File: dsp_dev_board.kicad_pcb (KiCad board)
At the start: 4 copper layers, 100 x 100 mm, 92 parts, among them J1 aux_mcu_power, J10 DX07S016JA1R1500, J11 Conn_02x11_Odd_Even, J2 audio_in, J3 audio_out, J4 9v_jack, J5 input_jack, J6 output_jack, J7 digital, J8 analog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

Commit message: pcb: minor movements, add more labels
more silkscreens, move some traces
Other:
- board text added: "3.3V"
- board text added: "GND"
- board text added: "WM8731"
- board text added: "audio in"
- board text added: "audio out"
- board text added: "input"
- board text added: "output"
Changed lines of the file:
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@@
   (general
     (thickness 1.6)
-    (drawings 47)
-    (tracks 806)
+    (drawings 55)
+    (tracks 810)
     (zones 0)
     (modules 92)
@@
     (tags resistor)
     (attr smd)
-    (fp_text reference R4 (at 0 -1.43) (layer F.SilkS)
+    (fp_text reference R4 (at -0.025 1.5) (layer F.SilkS)
       (effects (font (size 1 1) (thickness 0.15)))
     )
@@
     (descr "Through hole straight pin header, 1x02, 2.54mm pitch, single row")
     (tags "Through hole pin header THT 1x02 2.54mm single row")
-    (fp_text reference J2 (at 3.2 0) (layer F.SilkS)
+    (fp_text reference J2 (at 0 5.2) (layer F.SilkS)
       (effects (font (size 1 1) (thickness 0.15)))
     )
@@
     (descr "Through hole straight pin header, 1x02, 2.54mm pitch, single row")
     (tags "Through hole pin header THT 1x02 2.54mm single row")
-    (fp_text reference J1 (at 3.1 0) (layer F.SilkS)
+    (fp_text reference J1 (at 0 5.2) (layer F.SilkS)
       (effects (font (size 1 1) (thickness 0.15)))
     )
@@
     )
   )
+  (gr_text output (at 100.4 68.5) (layer F.SilkS)
+    (effects (font (size 1 1) (thickness 0.15)))
+  )
+  (gr_text input (at 185.4 68.4) (layer F.SilkS)
+    (effects (font (size 1 1) (thickness 0.15)))
+  )
+  (gr_text GND (at 163.3 47.2) (layer F.SilkS)
+    (effects (font (size 1 1) (thickness 0.15)) (justify left))
+  )
+  (gr_text 3.3V (at 163.3 44.5325) (layer F.SilkS)
+    (effects (font (size 1 1) (thickness 0.15)) (justify left))
+  )
+  (gr_text "audio in" (at 173.5 69.8) (layer F.SilkS)
+    (effects (font (size 1 1) (thickness 0.15)) (justify left))
+  )
+  (gr_text WM8731 (at 163.2 79.5) (layer F.SilkS)
+    (effects (font (size 1 1) (thickness 0.15)) (justify left))
+  )
+  (gr_text GND (at 148.8275 70.1 -90) (layer F.SilkS)
+    (effects (font (size 1 1) (thickness 0.15)) (justify left))
+  )
+  (gr_text "audio out" (at 151.3675 70.1 -90) (layer F.SilkS)
+    (effects (font (size 1 1) (thickness 0.15)) (justify left))
+  )
   (gr_text PB07 (at 97.6 97.4125) (layer F.SilkS)
     (effects (font (size 1 1) (thickness 0.15)) (justify left))
@@
   (segment (start 153.631666 59.495) (end 154.125 59.495) (width 0.25) (layer F.Cu) (net 9) (status 30))
   (segment (start 149.02001 59.85001) (end 147.97 58.8) (width 0.25) (layer F.Cu) (net 9) (status 20))
-  (segment (start 153.76999 59.85001) (end 149.02001 59.85001) (width 0.25) (layer F.Cu) (net 9))
-  (segment (start 154.125 59.495) (end 153.76999 59.85001) (width 0.25) (layer F.Cu) (net 9) (status 10))
   (segment (start 148.315 60.585) (end 148.315 60.783334) (width 0.25) (layer F.Cu) (net 9) (status 30))
   (segment (start 149.02001 59.87999) (end 148.315 60.585) (width 0.25) (layer F.Cu) (net 9) (status 20))
   (segment (start 149.02001 59.85001) (end 149.02001 59.87999) (width 0.25) (layer F.Cu) (net 9))
+  (segment (start 149.64999 59.85001) (end 149.02001 59.85001) (width 0.25) (layer F.Cu) (net 9))
+  (segment (start 150.73999 59.85001) (end 149.64999 59.85001) (width 0.25) (layer F.Cu) (net 9))
+  (segment (start 154.125 59.495) (end 151.095 59.495) (width 0.25) (layer F.Cu) (net 9))
+  (segment (start 151.095 59.495) (end 150.73999 59.85001) (width 0.25) (layer F.Cu) (net 9))
   (segment (start 103.574999 60.225001) (end 93 60.225001) (width 0.25) (layer F.Cu) (net 10) (status 20))
   (segment (start 119.4 44.4) (end 103.574999 60.225001) (width 0.25) (layer F.Cu) (net 10))
@@
   (via (at 148.65 47.5) (size 0.4) (drill 0.3) (layers F.Cu B.Cu) (net 32))
   (segment (start 148.65 46.2) (end 148.65 47.45) (width 0.25) (layer F.Cu) (net 32) (status 10))
-  (segment (start 148.65 47.5) (end 145.474999 50.675001) (width 0.25) (layer B.Cu) (net 32))
-  (segment (start 145.474999 50.675001) (end 145.474999 52.725007) (width 0.25) (layer B.Cu) (net 32))
   (via (at 121.3 76.900006) (size 0.4) (drill 0.3) (layers F.Cu B.Cu) (net 32))
-  (segment (start 145.474999 52.725007) (end 121.3 76.900006) (width 0.25) (layer B.Cu) (net 32))
   (segment (start 121 77.200006) (end 121.3 76.900006) (width 0.25) (layer F.Cu) (net 32))
   (segment (start 121 78.8875) (end 121 77.200006) (width 0.25) (layer F.Cu) (net 32) (status 10))
+  (segment (start 145.3 52.900006) (end 121.3 76.900006) (width 0.25) (layer B.Cu) (net 32))
+  (segment (start 148.65 47.5) (end 145.3 50.85) (width 0.25) (layer B.Cu) (net 32))
+  (segment (start 145.3 50.85) (end 145.3 52.900006) (width 0.25) (layer B.Cu) (net 32))
   (segment (start 150.65 47.85) (end 150.65 46.2) (width 0.25) (layer F.Cu) (net 35) (status 20))
   (segment (start 149 49.5) (end 150.65 47.85) (width 0.25) (layer F.Cu) (net 35) (status 10))
@@
   (segment (start 156.83 62.035) (end 154.125 62.035) (width 0.25) (layer F.Cu) (net 44) (status 20))
   (segment (start 159.075 63.305) (end 158.1 63.305) (width 0.25) (layer F.Cu) (net 44) (status 30))
-  (segment (start 155.5 60.705) (end 156.9475 62.1525) (width 0.25) (layer F.Cu) (net 44))
-  (segment (start 155.5 56.3) (end 155.5 60.705) (width 0.25) (layer F.Cu) (net 44) (status 10))
   (segment (start 156.9475 62.1525) (end 156.83 62.035) (width 0.25) (layer F.Cu) (net 44))
   (segment (start 158.1 63.305) (end 156.9475 62.1525) (width 0.25) (layer F.Cu) (net 44) (status 10))
+  (segment (start 156.8475 62.0525) (end 156.9475 62.1525) (width 0.25) (layer F.Cu) (net 44))
+  (segment (start 156.8475 59.8475) (end 156.8475 62.0525) (width 0.25) (layer F.Cu) (net 44))
+  (segment (start 155.5 56.3) (end 155.5 58.5) (width 0.25) (layer F.Cu) (net 44))
+  (segment (start 155.5 58.5) (end 156.8475 59.8475) (width 0.25) (layer F.Cu) (net 44))
   (segment (start 165.125 58.925) (end 165.125 60.5) (width 0.25) (layer F.Cu) (net 45) (status 30))
   (via (at 161 62) (size 0.4) (drill 0.3) (layers F.Cu B.Cu) (net 45))
@@
   (segment (start 95.8 84.78) (end 99.019999 87.999999) (width 0.25) (layer B.Cu) (net 73) (status 10))
   (segment (start 99.019999 87.999999) (end 115.399999 87.999999) (width 0.25) (layer B.Cu) (net 73))
-  (segment (start 115.599998 87.8) (end 115.399999 87.999999) (width 0.25) (layer F.Cu) (net 73))
-  (segment (start 118.0875 87.8) (end 115.599998 87.8) (width 0.25) (layer F.Cu) (net 73) (status 10))
   (via (at 115.399999 87.999999) (size 0.4) (drill 0.3) (layers F.Cu B.Cu) (net 73))
-  (segment (start 100.66 87.1) (end 115.399934 87.1) (width 0.25) (layer B.Cu) (net 74))
-  (segment (start 118.0875 87.3) (end 115.599933 87.299999) (width 0.25) (layer F.Cu) (net 74) (status 10))
-  (segment (start 115.599933 87.299999) (end 115.399934 87.1) (width 0.25) (layer F.Cu) (net 74))
-  (segment (start 95.8 82.24) (end 100.66 87.1) (width 0.25) (layer B.Cu) (net 74) (status 10))
-  (via (at 115.399934 87.1) (size 0.4) (drill 0.3) (layers F.Cu B.Cu) (net 74))
+  (segment (start 118.0875 87.8) (end 115.87694 87.8) (width 0.25) (layer F.Cu) (net 73))
+  (segment (start 115.87694 87.8) (end 115.676941 87.999999) (width 0.25) (layer F.Cu) (net 73))
+  (segment (start 115.676941 87.999999) (end 115.399999 87.999999) (width 0.25) (layer F.Cu) (net 73))
+  (segment (start 118.0875 87.3) (end 115.399926 87.3) (width 0.25) (layer F.Cu) (net 74))
+  (via (at 115.399926 87.3) (size 0.4) (drill 0.3) (layers F.Cu B.Cu) (net 74))
+  (segment (start 100.86 87.3) (end 115.399926 87.3) (width 0.25) (layer B.Cu) (net 74))
+  (segment (start 95.8 82.24) (end 100.86 87.3) (width 0.25) (layer B.Cu) (net 74))
   (segment (start 95.8 79.7) (end 108.60002 79.7) (width 0.25) (layer B.Cu) (net 75) (status 10))
   (segment (start 118.0875 86.8) (end 115.911611 86.8) (width 0.25) (layer F.Cu) (net 75) (status 10))

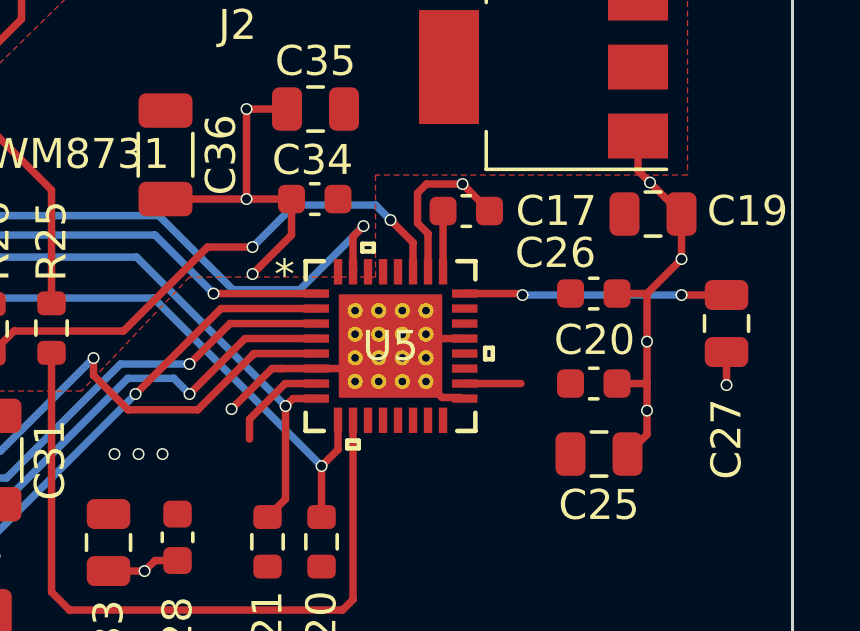
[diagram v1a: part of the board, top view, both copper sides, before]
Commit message: Swap TI codec footprint for builtin QFN
5x5mm size, 0.5mm pitch, 3.45mm exposed pad.  TI recommends the thermal
vias, though on something this low-power, I think that's overkill.

I had to use a copper-fill keepout and manually draw traces to keep the
pads from being horribly misshaped.
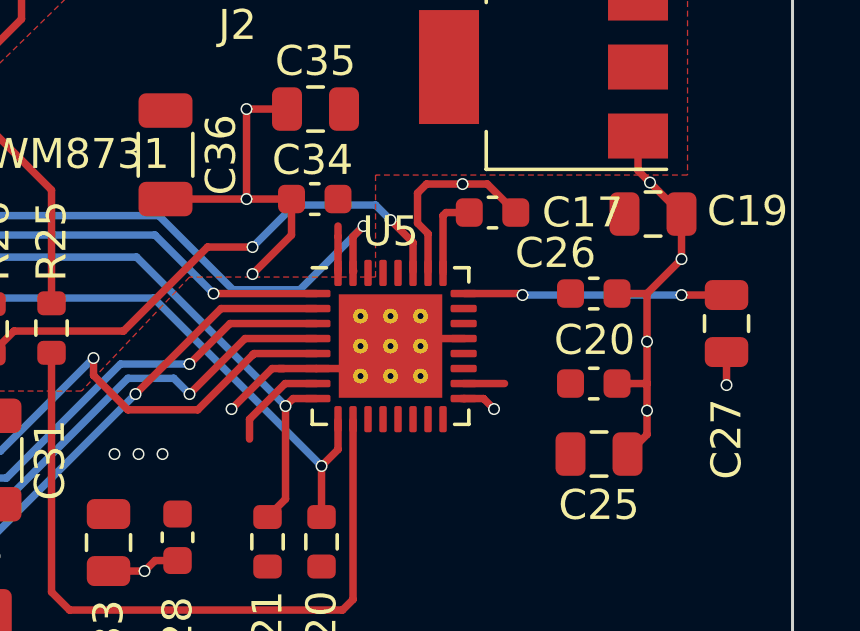
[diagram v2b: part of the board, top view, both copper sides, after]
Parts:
- U5: footprint TLV320AIC3105:TLV320AIC3105IRHBR -> Package_DFN_QFN:QFN-32-1EP_5x5mm_P0.5mm_EP3.45x3.45mm_ThermalVias
- moved C17 0.88 mm to (180.0, 81.5)
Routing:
- net 1.8V: track 0.00 -> 1.56 mm
- net GND: track 183.7 -> 182.8 mm, vias 44 -> 45

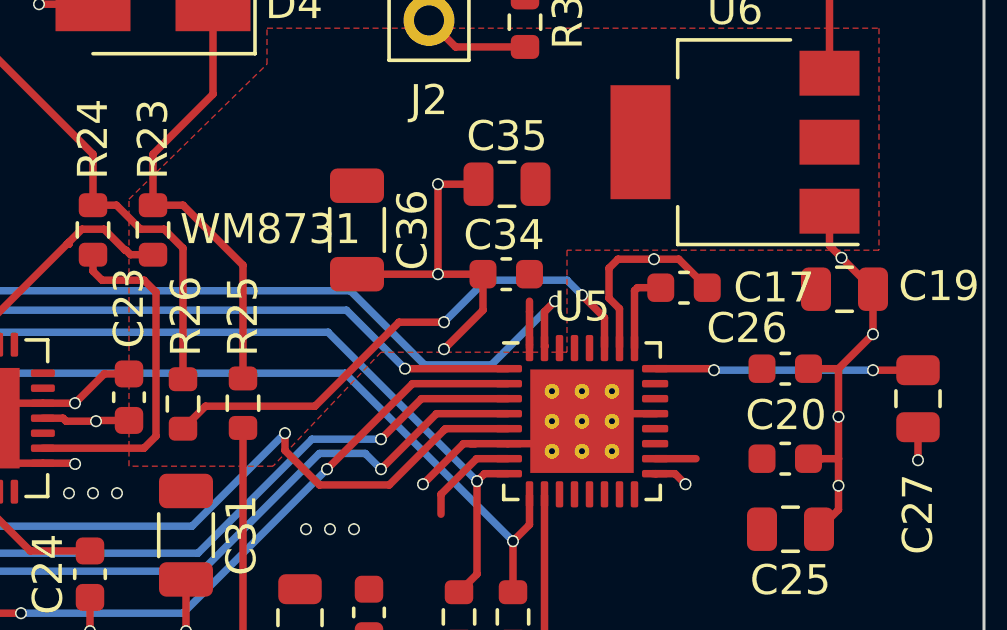
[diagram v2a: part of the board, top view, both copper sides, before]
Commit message: pcb: move more silkscreens
I moved C17, so its silkscreen ended up under C19.

Label the jumpers for WM and TI codecs (and abbreviate to WM because
"WM8731" doesn't fit in the space I have)
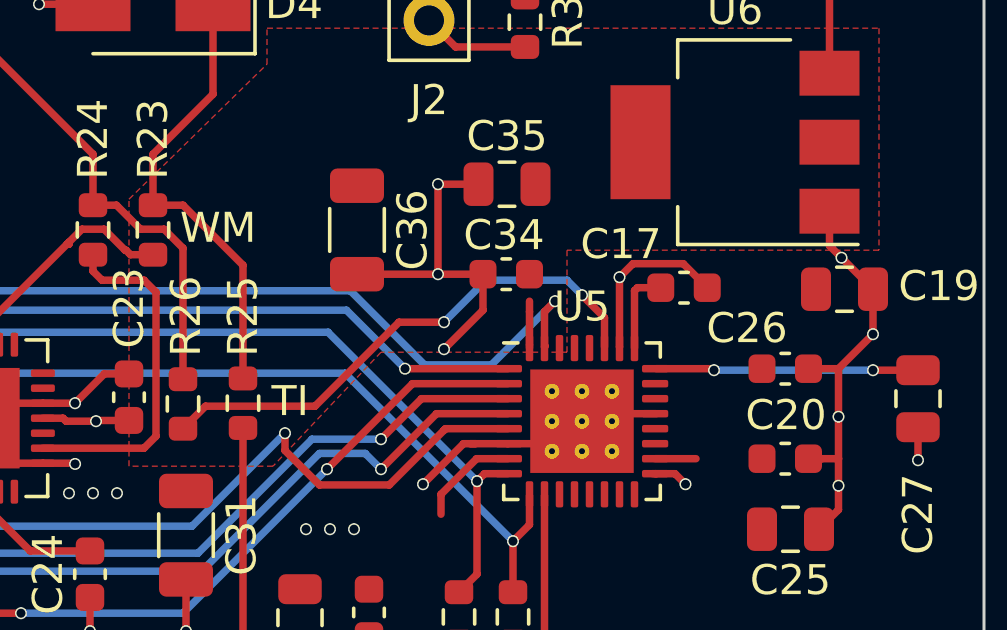
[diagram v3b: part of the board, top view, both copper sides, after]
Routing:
- net GND: track 182.8 -> 182.0 mm
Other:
- board text added: "TI"
- board text added: "WM"
- board text removed: "WM8731"

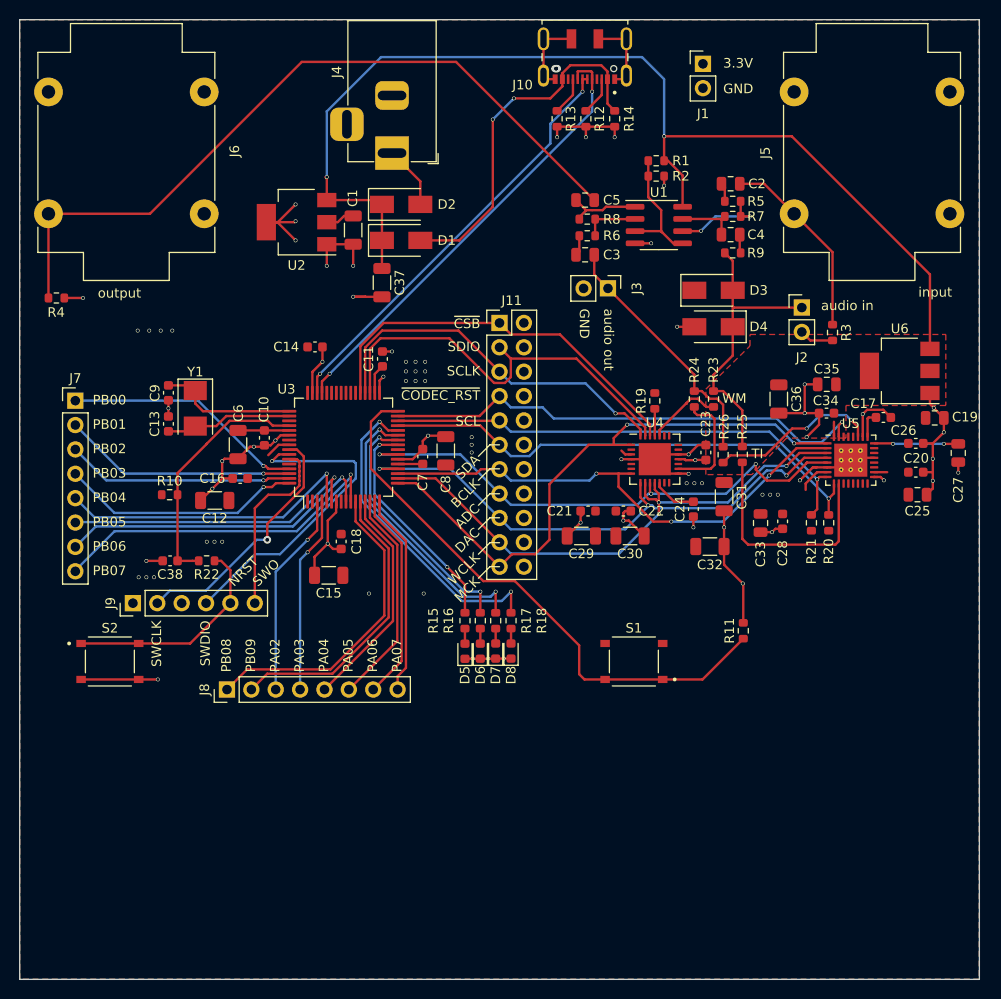
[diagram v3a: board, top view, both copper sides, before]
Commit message: power should be center-negative
And add attribution text to the PCB
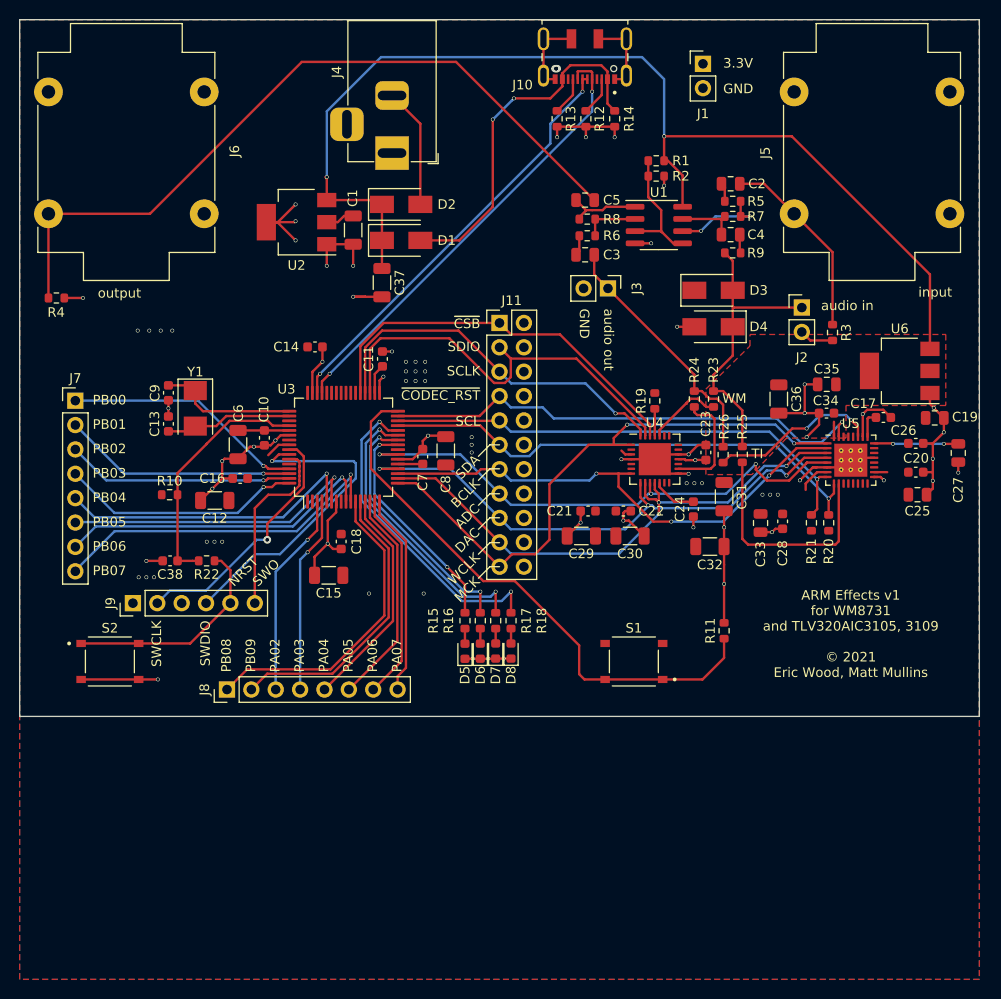
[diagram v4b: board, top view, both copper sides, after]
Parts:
- moved R11 2.00 mm to (163.4, 103.7)
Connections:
- J4 pad 1: Net-(D2-Pad2) -> GND
- J4 pad 2: GND -> Net-(D2-Pad2)
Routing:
- net Net-(D2-Pad2): track 6.57 -> 12.6 mm
- net GND: track 182.0 -> 181.2 mm
- net /MCU/BOOT0: track 59.6 -> 58.8 mm
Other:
- board size 100 x 100 mm -> 100 x 72.6 mm
- board text added: "ARM Effects v1 for WM8731 and TLV320AIC3105, 3109 © 2021 Eric Wood, Matt Mullins"
